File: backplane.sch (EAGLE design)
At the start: 3 parts, among them J101 80-PIN-CARD-EDGE, J201 80-PIN-CARD-EDGE, J301 80-PIN-CARD-EDGE

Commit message: Updates and fixes
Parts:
- removed J101: 80-PIN-CARD-EDGE, auv:80-PIN-CARD-EDGE
- added U$1: JETSON_CARRIER, auv:JETSON_CARRIER
- added U401: USB3150, auv:USB3150
- J201, J301: value 80-PIN-CARD-EDGE -> TE-2-5530843-0; device auv:80-PIN-CARD-EDGE -> auv:TE-2-5530843-0
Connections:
- new net GND: U$1.GND
- new net JETSON_GPIO0: U$1.GPIO0
- new net JETSON_GPIO1: U$1.GPIO1
- new net JETSON_GPIO2: U$1.GPIO2
- new net JETSON_GPIO3: U$1.GPIO3
- new net JETSON_I2C_SCL: U$1.I2C_SCL
- new net JETSON_I2C_SDA: U$1.I2C_SDA
- new net JETSON_PWR_BTN: U$1.PWR_BTN
- new net JETSON_UART1_RX: U$1.UART1_RX
- new net JETSON_UART1_TX: U$1.UART1_TX
- new net PIXHAWK_TELEM2_RX: U$1.UART0_TX
- new net PIXHAWK_TELEM2_TX: U$1.UART0_RX
- new net VBAT: U$1.VIN
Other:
- note added: "USB Hub"
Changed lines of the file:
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@@
 <?xml version="1.0" encoding="utf-8"?>
 <!DOCTYPE eagle SYSTEM "eagle.dtd">
-<eagle version="8.4.0">
+<eagle version="8.6.1">
 <drawing>
 <settings>
@@
 <part name="FRAME2" library="auv" deviceset="FRAME_A_L" device=""/>
 <part name="FRAME3" library="auv" deviceset="FRAME_A_L" device=""/>
-<part name="J101" library="auv" deviceset="80-PIN-CARD-EDGE" device=""/>
-<part name="J201" library="auv" deviceset="80-PIN-CARD-EDGE" device=""/>
-<part name="J301" library="auv" deviceset="80-PIN-CARD-EDGE" device=""/>
+<part name="J201" library="auv" deviceset="TE-2-5530843-0" device=""/>
+<part name="J301" library="auv" deviceset="TE-2-5530843-0" device=""/>
+<part name="FRAME4" library="auv" deviceset="FRAME_A_L" device=""/>
+<part name="U401" library="auv" deviceset="USB3150" device=""/>
+<part name="U$1" library="auv" deviceset="JETSON_CARRIER" device=""/>
+<part name="GND1" library="auv" deviceset="GND" device=""/>
 </parts>
 <sheets>
@@
 <instance part="FRAME1" gate="G$1" x="0" y="0"/>
 <instance part="FRAME1" gate="G$2" x="172.72" y="0"/>
-<instance part="J101" gate="G$1" x="152.4" y="107.95"/>
+<instance part="U$1" gate="G$1" x="134.62" y="114.3"/>
+<instance part="GND1" gate="1" x="149.86" y="91.44"/>
 </instances>
 <busses>
 </busses>
 <nets>
+<net name="VBAT" class="0">
+<segment>
+<pinref part="U$1" gate="G$1" pin="VIN"/>
+<wire x1="147.32" y1="129.54" x2="152.4" y2="129.54" width="0.1524" layer="91"/>
+<label x="152.4" y="129.54" size="1.27" layer="95" xref="yes"/>
+</segment>
+</net>
+<net name="JETSON_PWR_BTN" class="0">
+<segment>
+<pinref part="U$1" gate="G$1" pin="PWR_BTN"/>
+<wire x1="147.32" y1="127" x2="152.4" y2="127" width="0.1524" layer="91"/>
+<label x="152.4" y="127" size="1.27" layer="95" xref="yes"/>
+</segment>
+</net>
+<net name="PIXHAWK_TELEM2_TX" class="0">
+<segment>
+<pinref part="U$1" gate="G$1" pin="UART0_RX"/>
+<wire x1="147.32" y1="124.46" x2="152.4" y2="124.46" width="0.1524" layer="91"/>
+<label x="152.4" y="124.46" size="1.27" layer="95" xref="yes"/>
+</segment>
+</net>
+<net name="PIXHAWK_TELEM2_RX" class="0">
+<segment>
+<pinref part="U$1" gate="G$1" pin="UART0_TX"/>
+<wire x1="147.32" y1="121.92" x2="152.4" y2="121.92" width="0.1524" layer="91"/>
+<label x="152.4" y="121.92" size="1.27" layer="95" xref="yes"/>
+</segment>
+</net>
+<net name="JETSON_UART1_RX" class="0">
+<segment>
+<pinref part="U$1" gate="G$1" pin="UART1_RX"/>
+<wire x1="147.32" y1="119.38" x2="152.4" y2="119.38" width="0.1524" layer="91"/>
+<label x="152.4" y="119.38" size="1.27" layer="95" xref="yes"/>
+</segment>
+</net>
+<net name="JETSON_UART1_TX" class="0">
+<segment>
+<pinref part="U$1" gate="G$1" pin="UART1_TX"/>
+<wire x1="147.32" y1="116.84" x2="152.4" y2="116.84" width="0.1524" layer="91"/>
+<label x="152.4" y="116.84" size="1.27" layer="95" xref="yes"/>
+</segment>
+</net>
+<net name="JETSON_GPIO1" class="0">
+<segment>
+<pinref part="U$1" gate="G$1" pin="GPIO1"/>
+<wire x1="147.32" y1="114.3" x2="152.4" y2="114.3" width="0.1524" layer="91"/>
+<label x="152.4" y="114.3" size="1.27" layer="95" xref="yes"/>
+</segment>
+</net>
+<net name="JETSON_GPIO0" class="0">
+<segment>
+<pinref part="U$1" gate="G$1" pin="GPIO0"/>
+<wire x1="147.32" y1="111.76" x2="152.4" y2="111.76" width="0.1524" layer="91"/>
+<label x="152.4" y="111.76" size="1.27" layer="95" xref="yes"/>
+</segment>
+</net>
+<net name="JETSON_GPIO3" class="0">
+<segment>
+<pinref part="U$1" gate="G$1" pin="GPIO3"/>
+<wire x1="147.32" y1="109.22" x2="152.4" y2="109.22" width="0.1524" layer="91"/>
+<label x="152.4" y="109.22" size="1.27" layer="95" xref="yes"/>
+</segment>
+</net>
+<net name="JETSON_GPIO2" class="0">
+<segment>
+<pinref part="U$1" gate="G$1" pin="GPIO2"/>
+<wire x1="147.32" y1="106.68" x2="152.4" y2="106.68" width="0.1524" layer="91"/>
+<label x="152.4" y="106.68" size="1.27" layer="95" xref="yes"/>
+</segment>
+</net>
+<net name="JETSON_I2C_SDA" class="0">
+<segment>
+<pinref part="U$1" gate="G$1" pin="I2C_SDA"/>
+<wire x1="147.32" y1="104.14" x2="152.4" y2="104.14" width="0.1524" layer="91"/>
+<label x="152.4" y="104.14" size="1.27" layer="95" xref="yes"/>
+</segment>
+</net>
+<net name="JETSON_I2C_SCL" class="0">
+<segment>
+<pinref part="U$1" gate="G$1" pin="I2C_SCL"/>
+<wire x1="147.32" y1="101.6" x2="152.4" y2="101.6" width="0.1524" layer="91"/>
+<label x="152.4" y="101.6" size="1.27" layer="95" xref="yes"/>
+</segment>
+</net>
+<net name="GND" class="0">
+<segment>
+<pinref part="U$1" gate="G$1" pin="GND"/>
+<pinref part="GND1" gate="1" pin="GND"/>
+<wire x1="147.32" y1="99.06" x2="149.86" y2="99.06" width="0.1524" layer="91"/>
+<wire x1="149.86" y1="99.06" x2="149.86" y2="93.98" width="0.1524" layer="91"/>
+</segment>
+</net>
 </nets>
 </sheet>
@@
 </instances>
 <busses>
+</busses>
+<nets>
+</nets>
+</sheet>
+<sheet>
+<plain>
+<text x="175.26" y="25.4" size="6.4516" layer="94">USB Hub</text>
+</plain>
+<instances>
+<instance part="FRAME4" gate="G$1" x="0" y="0"/>
+<instance part="FRAME4" gate="G$2" x="172.72" y="0"/>
+<instance part="U401" gate="G$1" x="116.84" y="127"/>
+</instances>
+<busses>

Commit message: Move jetson to the backplane
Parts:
- removed U401: USB3150, auv:USB3150
- added HUB_PWR: USB3150-30-130-A, auv:USB3150-30-130-A
- added PWM: (no value), auv:PINHD-2X10
- added PWR, REC, RST: (no value), auv:TAC_SWITCHPTH
- added U$3: ORBITTY_CARRIER, auv:ORBITTY_CARRIER
- U$1: value JETSON_CARRIER -> AHRS8P; device auv:JETSON_CARRIER -> auv:AHRS8P
- renumbered J201 to POWER, J301 to PIXHAWK
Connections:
- removed net JETSON_GPIO0: U$1.GPIO0
- removed net JETSON_GPIO1: U$1.GPIO1
- removed net JETSON_GPIO2: U$1.GPIO2
- removed net JETSON_GPIO3: U$1.GPIO3
- removed net JETSON_I2C_SCL: U$1.I2C_SCL
- removed net JETSON_I2C_SDA: U$1.I2C_SDA
- removed net JETSON_PWR_BTN: U$1.PWR_BTN
- removed net JETSON_UART1_RX: U$1.UART1_RX
- removed net JETSON_UART1_TX: U$1.UART1_TX
- new net +5V: HUB_PWR.VBUS, U$1.VIN
- new net AHRS8_RX: U$1.RX
- new net AHRS8_TX: U$1.TX
- new net N$3: PWR.3, PWR.4, U$3.POWER_BUTTON
- new net N$4: RST.3, RST.4, U$3.RESET
- new net N$5: REC.3, REC.4, U$3.RECOVERY
- new net PWR: PWR.1, PWR.2
- new net SPARTON_RX: U$3.UART0_TX
- new net SPARTON_TX: U$3.UART0_RX
- net GND: now also HUB_PWR.GND, HUB_PWR.SHIELD, PWM.1, PWM.11, PWM.13, PWM.15, PWM.17, PWM.19, PWM.3, PWM.5, PWM.7, PWM.9, REC.1, REC.2, RST.1, RST.2, U$3.GND
- net PIXHAWK_TELEM2_RX: now also U$3.UART1_TX; no longer U$1.UART0_TX
- net PIXHAWK_TELEM2_TX: now also U$3.UART1_RX; no longer U$1.UART0_RX
- net VBAT: now also U$3.VIN; no longer U$1.VIN
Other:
- note added: "Misc"
- note removed: "USB Hub"

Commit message: Update backplane
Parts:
- POWER: value TE-2-5530843-0 -> TE-5-5530843-0; device auv:TE-2-5530843-0 -> auv:TE-5-5530843-0
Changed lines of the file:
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@@
 <?xml version="1.0" encoding="utf-8"?>
 <!DOCTYPE eagle SYSTEM "eagle.dtd">
-<eagle version="8.6.3">
+<eagle version="8.7.1">
 <drawing>
 <settings>
@@
 <part name="FRAME2" library="auv" deviceset="FRAME_A_L" device=""/>
 <part name="FRAME3" library="auv" deviceset="FRAME_A_L" device=""/>
-<part name="POWER" library="auv" deviceset="TE-2-5530843-0" device=""/>
 <part name="PIXHAWK" library="auv" deviceset="TE-2-5530843-0" device=""/>
 <part name="FRAME4" library="auv" deviceset="FRAME_A_L" device=""/>
@@
 <part name="P+2" library="auv" deviceset="+5V" device=""/>
 <part name="GND7" library="auv" deviceset="GND" device=""/>
+<part name="POWER" library="auv" deviceset="TE-5-5530843-0" device=""/>
 </parts>
 <sheets>
@@
 <instance part="FRAME2" gate="G$1" x="0" y="0"/>
 <instance part="FRAME2" gate="G$2" x="172.72" y="0"/>
-<instance part="POWER" gate="G$1" x="152.4" y="107.95"/>
+<instance part="POWER" gate="G$1" x="132.08" y="109.22"/>
 </instances>
 <busses>

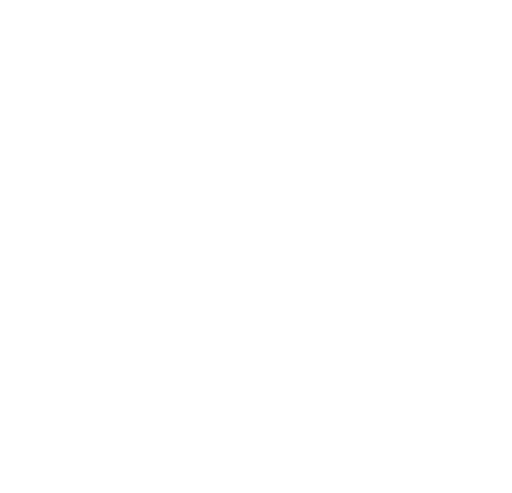
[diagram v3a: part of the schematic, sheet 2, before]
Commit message: Add XT60 connector
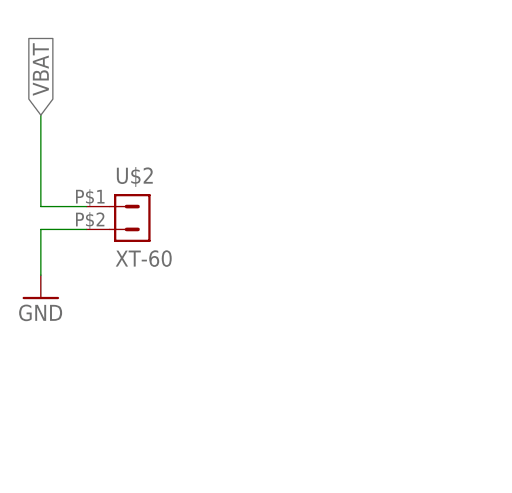
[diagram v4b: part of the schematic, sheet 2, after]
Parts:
- added U$2: XT-60, auv:XT-60
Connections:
- net GND: now also U$2.2
- net VBAT: now also U$2.1
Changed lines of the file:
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@@
 <part name="GND7" library="auv" deviceset="GND" device=""/>
 <part name="POWER" library="auv" deviceset="TE-5-5530843-0" device=""/>
+<part name="U$2" library="auv" deviceset="XT-60" device=""/>
+<part name="GND8" library="auv" deviceset="GND" device=""/>
 </parts>
 <sheets>
@@
 <instance part="FRAME2" gate="G$2" x="172.72" y="0"/>
 <instance part="POWER" gate="G$1" x="132.08" y="109.22"/>
+<instance part="U$2" gate="G$1" x="93.98" y="167.64"/>
+<instance part="GND8" gate="1" x="83.82" y="157.48"/>
 </instances>
 <busses>
 </busses>
 <nets>
+<net name="VBAT" class="0">
+<segment>
+<pinref part="U$2" gate="G$1" pin="1"/>
+<wire x1="88.9" y1="167.64" x2="83.82" y2="167.64" width="0.1524" layer="91"/>
+<wire x1="83.82" y1="167.64" x2="83.82" y2="177.8" width="0.1524" layer="91"/>
+<label x="83.82" y="177.8" size="1.778" layer="95" rot="R90" xref="yes"/>
+</segment>
+</net>
+<net name="GND" class="0">
+<segment>
+<pinref part="U$2" gate="G$1" pin="2"/>
+<wire x1="88.9" y1="165.1" x2="83.82" y2="165.1" width="0.1524" layer="91"/>
+<wire x1="83.82" y1="165.1" x2="83.82" y2="160.02" width="0.1524" layer="91"/>
+<pinref part="GND8" gate="1" pin="GND"/>
+</segment>
+</net>
 </nets>
 </sheet>

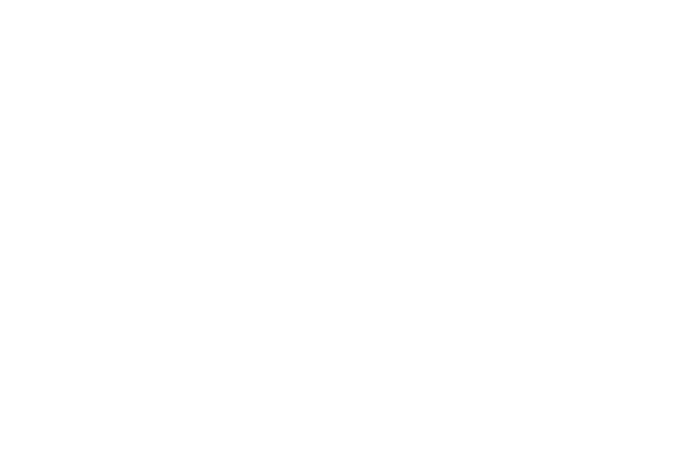
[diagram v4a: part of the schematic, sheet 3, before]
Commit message: Depth sensor I2C
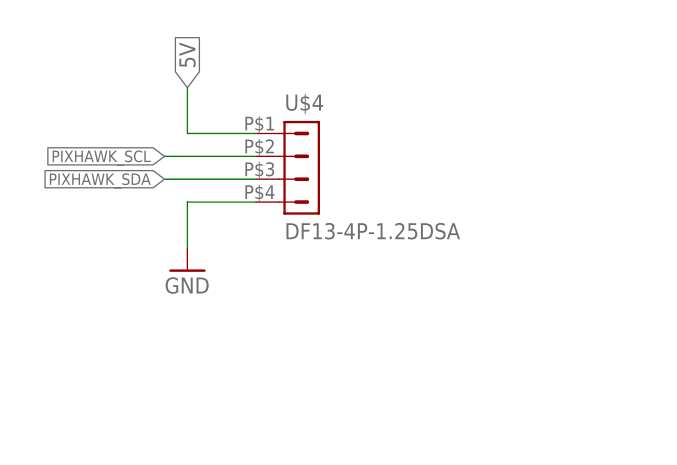
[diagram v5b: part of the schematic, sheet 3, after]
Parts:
- added U$4: DF13-4P-1.25DSA, auv:DF13-4P-1.25DSA
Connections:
- new net 5V: U$4.1
- new net PIXHAWK_SCL: U$4.2
- new net PIXHAWK_SDA: U$4.3
- net GND: now also U$4.4
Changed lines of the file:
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@@
 <part name="U$2" library="auv" deviceset="XT-60" device=""/>
 <part name="GND8" library="auv" deviceset="GND" device=""/>
+<part name="U$4" library="auv" deviceset="DF13-4P-1.25" device="DSA"/>
+<part name="GND9" library="auv" deviceset="GND" device=""/>
 </parts>
 <sheets>
@@
 <instance part="PWM" gate="A" x="71.12" y="111.76"/>
 <instance part="GND6" gate="1" x="58.42" y="91.44"/>
+<instance part="U$4" gate="G$1" x="73.66" y="172.72"/>
+<instance part="GND9" gate="1" x="60.96" y="160.02"/>
 </instances>
 <busses>
@@
 <pinref part="GND6" gate="1" pin="GND"/>
 </segment>
-</net>
+<segment>
+<pinref part="U$4" gate="G$1" pin="4"/>
+<wire x1="68.58" y1="167.64" x2="60.96" y2="167.64" width="0.1524" layer="91"/>
+<pinref part="GND9" gate="1" pin="GND"/>
+<wire x1="60.96" y1="167.64" x2="60.96" y2="162.56" width="0.1524" layer="91"/>
+</segment>
+</net>
+<net name="5V" class="0">
+<segment>
+<pinref part="U$4" gate="G$1" pin="1"/>
+<wire x1="68.58" y1="175.26" x2="60.96" y2="175.26" width="0.1524" layer="91"/>
+<wire x1="60.96" y1="175.26" x2="60.96" y2="180.34" width="0.1524" layer="91"/>
+<label x="60.96" y="180.34" size="1.778" layer="95" rot="R90" xref="yes"/>
+</segment>
+</net>
+<net name="PIXHAWK_SCL" class="0">
+<segment>
+<pinref part="U$4" gate="G$1" pin="2"/>
+<wire x1="68.58" y1="172.72" x2="58.42" y2="172.72" width="0.1524" layer="91"/>
+<label x="58.42" y="172.72" size="1.27" layer="95" rot="R180" xref="yes"/>
+</segment>
+</net>
+<net name="PIXHAWK_SDA" class="0">
+<segment>
+<pinref part="U$4" gate="G$1" pin="3"/>
+<wire x1="68.58" y1="170.18" x2="58.42" y2="170.18" width="0.1524" layer="91"/>
+<label x="58.42" y="170.18" size="1.27" layer="95" rot="R180" xref="yes"/>
+</segment>
+</net>
